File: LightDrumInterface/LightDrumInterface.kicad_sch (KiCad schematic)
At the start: 79 parts, among them J1 MIDI-IN, J2 0525593652, J2 Micro_SD_Card, J4 PWR-CONN, J5 MIDI-OUT, J6 0541323662, Q1 NX6008NBKWX, Q2 NX6008NBKWX, Q3 NX6008NBKWX, Q4 NX6008NBKWX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

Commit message: PCB Lock REV11
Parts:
- removed D-MD1, D-ML1, D-MR1, D-MU1: RED, LED_SMD:LED_0805_2012Metric, symbol Device:LED_Small
- added D2, D3: APHBM2012QBDSURKC, Daxxn_LEDs:APHBM-2012, symbol Daxxn_LEDs:APHBM2012QBDSURKC
- added H1, H2, H3, H4: M2.5, MountingHole:MountingHole_2.7mm_M2.5_Pad_Via, symbol Mechanical:MountingHole_Pad
- DA1: PartNumber (none) -> 0904-0001
- J2: value 0525593652 -> DNP; SupplierPN (none) -> WM7988CT-ND
- U4: PartNumber (none) -> 0802-0002
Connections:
- net SD-DAT0 is gone; now on net SD-D0: J2.7 (DAT0), R25.2
- net SD-DAT3/CD is gone; now on net SD-CD: J2.2 (DAT3/CD), R27.2
- net AUDIO-SRC-IND: now also J2.3 (Pin_3); no longer J2.4 (Pin_4)
- net DIAG-DEBUG: no longer J2.5 (Pin_5)
- net DIAG-STATUS: no longer J2.6 (Pin_6)
- net ENC1-A: now also J2.21 (Pin_21), J6.16 (Pin_16); no longer J2.28 (Pin_28), J6.9 (Pin_9)
- net ENC1-B: now also J2.14 (Pin_14), J6.23 (Pin_23); no longer J2.10 (Pin_10), J6.27 (Pin_27)
- net ENC2-A: now also J2.23 (Pin_23), J6.14 (Pin_14); no longer J2.26 (Pin_26), J6.11 (Pin_11)
- net ENC2-SW: now also J2.19 (Pin_19), J6.18 (Pin_18); no longer J2.22 (Pin_22), J6.15 (Pin_15)
- net GND: now also J2.32 (Pin_32), J6.5 (Pin_5), H1.1, H2.1, H3.1, H4.1; no longer J2.3 (Pin_3), J2.30 (Pin_30), J2.34 (Pin_34), J2.8 (Pin_8), J2.9 (Pin_9), J6.7 (Pin_7)
- net GRAPH-CLK: now also J6.6 (Pin_6); no longer J2.29 (Pin_29), J6.8 (Pin_8)
- net GRAPH-LE: now also J6.25 (Pin_25); no longer J2.14 (Pin_14), J6.23 (Pin_23)
- net GRAPH-SDI: now also J6.24 (Pin_24); no longer J2.31 (Pin_31), J6.6 (Pin_6)
- net GRAPH-~{OE}: now also J6.27 (Pin_27); no longer J2.12 (Pin_12), J6.25 (Pin_25)
- net I2C-SCLK: now also J6.15 (Pin_15); no longer J2.20 (Pin_20), J6.17 (Pin_17)
- net I2C-SDA: now also J6.13 (Pin_13); no longer J2.23 (Pin_23), J6.14 (Pin_14)
- net MENU-ACT: no longer J2.17 (Pin_17)
- net MENU-BACK: no longer J2.16 (Pin_16)
- net MENU-DOWN: no longer J2.11 (Pin_11)
- net MENU-LEFT: now also J6.8 (Pin_8); no longer J2.13 (Pin_13), J6.24 (Pin_24)
- net MENU-RIGHT: no longer J2.18 (Pin_18)
- net MENU-UP: no longer J2.15 (Pin_15)
- net MIDI-IN: now also J6.3 (Pin_3); no longer J2.32 (Pin_32), J6.5 (Pin_5)
- net MIDI-OUT: no longer J2.35 (Pin_35)
- net SCR-RX: now also J6.9 (Pin_9); no longer J2.19 (Pin_19), J6.18 (Pin_18)
- net SCR-TX: now also J6.7 (Pin_7); no longer J2.21 (Pin_21), J6.16 (Pin_16)
- net SD-CD: now also J6.17 (Pin_17); no longer J6.3 (Pin_3)
- net SD-CLK: now also J6.28 (Pin_28); no longer J6.29 (Pin_29)
- net SD-D0: now also J6.29 (Pin_29); no longer J6.28 (Pin_28)
- net STRIP-PWR: now also J2.6 (Pin_6); no longer J2.7 (Pin_7)
- net VCC: now also J2.26 (Pin_26), J6.11 (Pin_11), D2.1 (B-A), D2.4 (R-A), D3.1 (B-A), D3.4 (R-A); no longer J2.24 (Pin_24), J6.13 (Pin_13)
- net ~{RESET}: no longer J2.33 (Pin_33)
- net at U1.17 (~{OUT12}): now also D2.2 (B-K)
- net at U1.18 (~{OUT13}): now also D2.3 (R-K)
- net at DA1.11: now also U1.14 (~{OUT9}); no longer U1.13 (~{OUT8})
- net at U1.15 (~{OUT10}): now also D3.2 (B-K)
- net at DA1.12: now also U1.13 (~{OUT8}); no longer U1.14 (~{OUT9})
- net at U1.16 (~{OUT11}): now also D3.3 (R-K)
- new net DIAG-DEBUG_{PWM}: J2.4 (Pin_4)
- new net DIAG-STATUS_{PWM}: J2.5 (Pin_5)
- new net GRAPH-CLK_{S}: J2.31 (Pin_31)
- new net GRAPH-LE_{S}: J2.12 (Pin_12)
- new net GRAPH-SDI_{S}: J2.13 (Pin_13)
- new net GRAPH-~{OE}_{S}: J2.10 (Pin_10)
- new net I2C-SCLK_{S}: J2.22 (Pin_22)
- new net I2C-SDA_{S}: J2.24 (Pin_24)
- new net MENU-ACT_{INT}: J2.17 (Pin_17)
- new net MENU-BACK_{INT}: J2.16 (Pin_16)
- new net MENU-DOWN_{INT}: J2.11 (Pin_11)
- new net MENU-LEFT_{INT}: J2.29 (Pin_29)
- new net MENU-RIGHT_{INT}: J2.18 (Pin_18)
- new net MENU-UP_{INT}: J2.15 (Pin_15)
- new net MIDI-IN_{S}: J2.34 (Pin_34)
- new net MIDI-OUT_{S}: J2.35 (Pin_35)
- new net SCR-RX_{S}: J2.28 (Pin_28)
- new net SCR-TX_{S}: J2.30 (Pin_30)
- new net SD-CD_{S}: J2.20 (Pin_20)
- new net SD-CLK_{S}: J2.9 (Pin_9)
- new net SD-CMD_{S}: J2.7 (Pin_7)
- new net SD-D0_{S}: J2.8 (Pin_8)
- new net ~{RESET}_{C}: J2.33 (Pin_33)
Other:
- note added: "ENCODER SELECT"
- note added: "MATCHING CONN ON MAIN PCB -NOT POPULATED-"
- note removed: "MATCHING CONN ON MAIN PCB NOT POPULATED"
- moved on the sheet: DA1I, DA1J

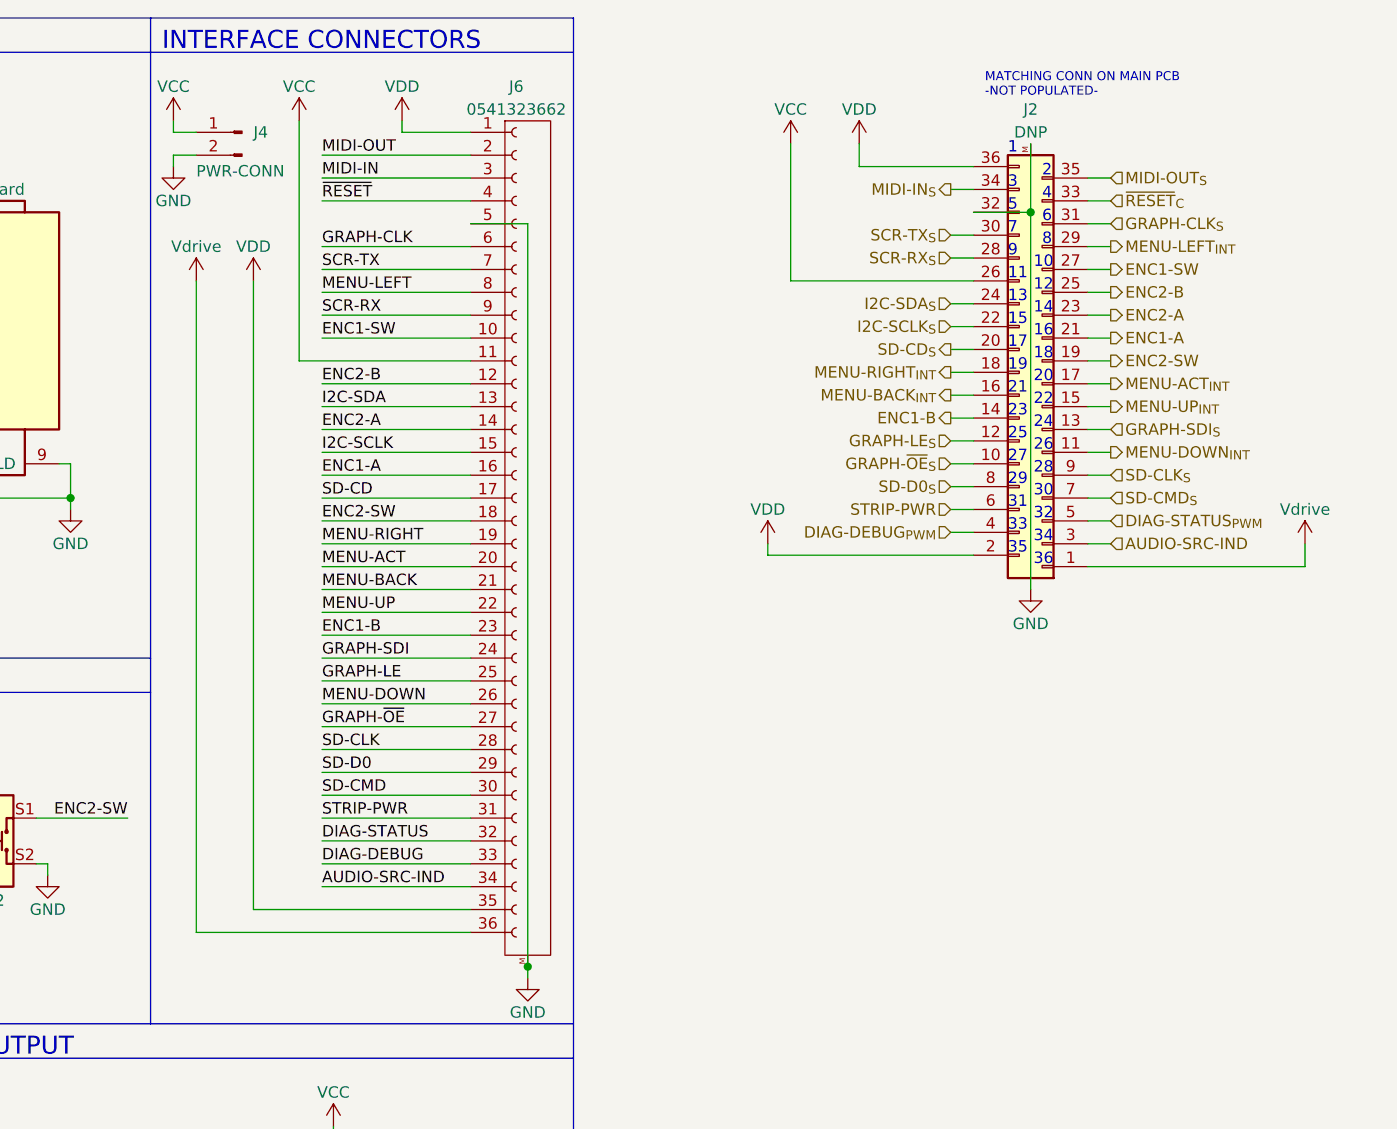
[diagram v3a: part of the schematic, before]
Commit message: Fix backwards Connector - Initial Testing
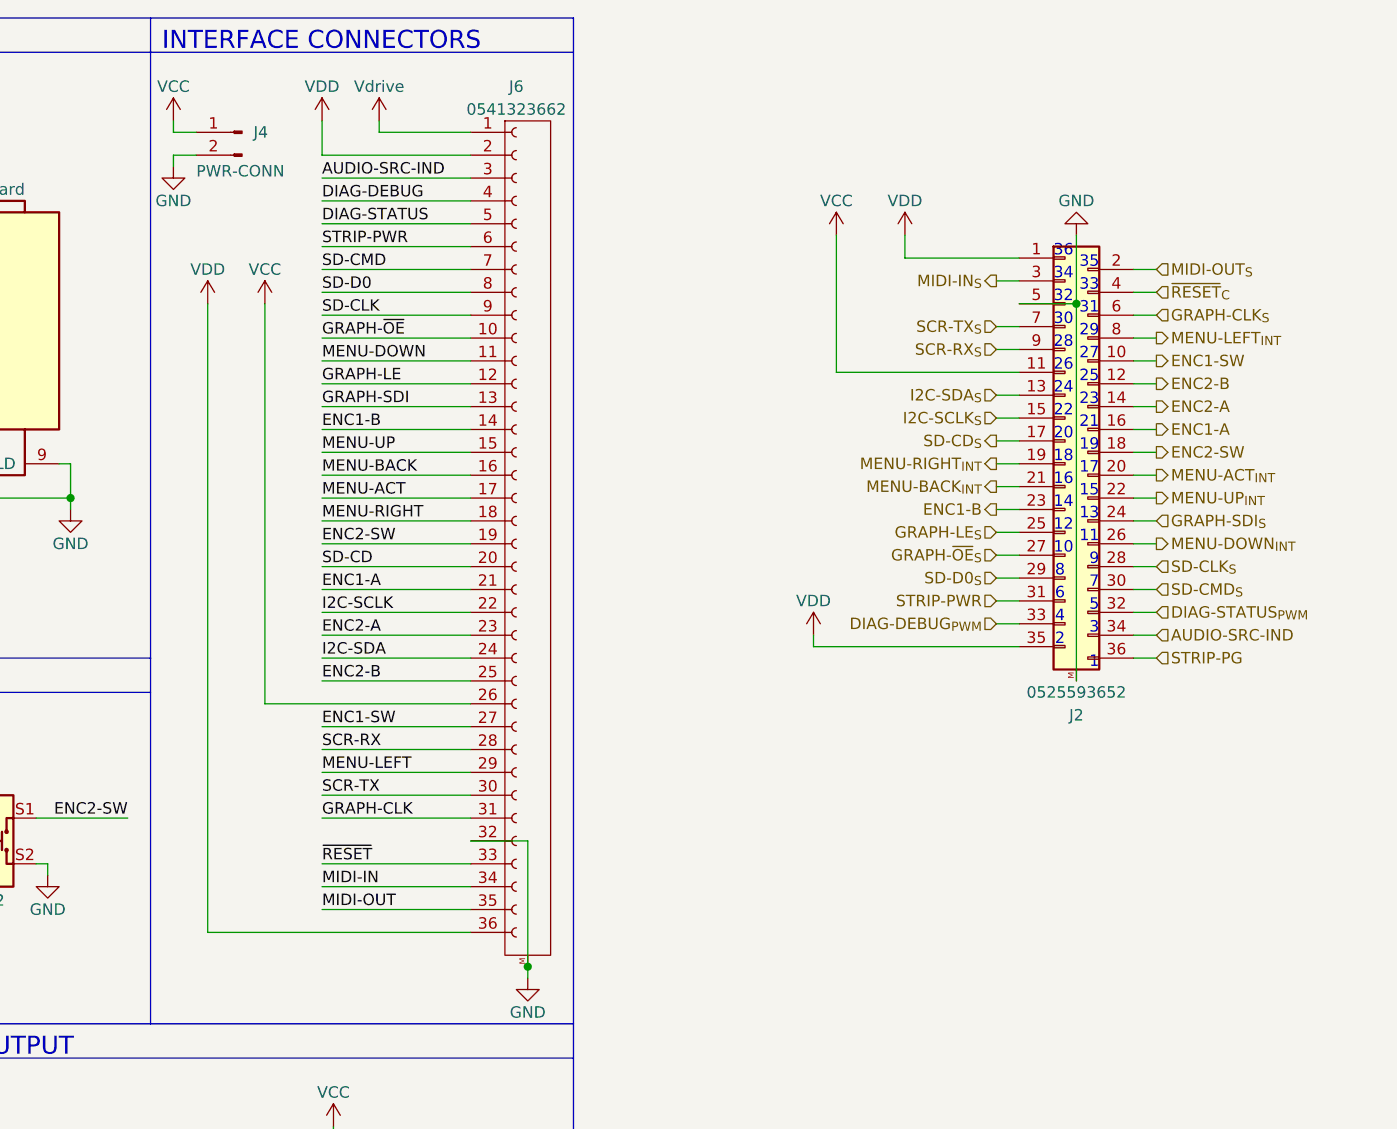
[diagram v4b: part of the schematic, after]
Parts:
- J2: value DNP -> 0525593652
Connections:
- net AUDIO-SRC-IND: now also J2.34 (Pin_34), J6.3 (Pin_3); no longer J2.3 (Pin_3), J6.34 (Pin_34)
- net DIAG-DEBUG: now also J6.4 (Pin_4); no longer J6.33 (Pin_33)
- net DIAG-DEBUG_{PWM}: now also J2.33 (Pin_33); no longer J2.4 (Pin_4)
- net DIAG-STATUS: now also J6.5 (Pin_5); no longer J6.32 (Pin_32)
- net DIAG-STATUS_{PWM}: now also J2.32 (Pin_32); no longer J2.5 (Pin_5)
- net ENC1-A: now also J2.16 (Pin_16), J6.21 (Pin_21); no longer J2.21 (Pin_21), J6.16 (Pin_16)
- net ENC1-B: now also J2.23 (Pin_23), J6.14 (Pin_14); no longer J2.14 (Pin_14), J6.23 (Pin_23)
- net ENC1-SW: now also J2.10 (Pin_10), J6.27 (Pin_27); no longer J2.27 (Pin_27), J6.10 (Pin_10)
- net ENC2-A: now also J2.14 (Pin_14), J6.23 (Pin_23); no longer J2.23 (Pin_23), J6.14 (Pin_14)
- net ENC2-B: now also J2.12 (Pin_12), J6.25 (Pin_25); no longer J2.25 (Pin_25), J6.12 (Pin_12)
- net ENC2-SW: now also J2.18 (Pin_18), J6.19 (Pin_19); no longer J2.19 (Pin_19), J6.18 (Pin_18)
- net GND: now also J2.5 (Pin_5), J6.32 (Pin_32); no longer J2.32 (Pin_32), J6.5 (Pin_5)
- net GRAPH-CLK: now also J6.31 (Pin_31); no longer J6.6 (Pin_6)
- net GRAPH-CLK_{S}: now also J2.6 (Pin_6); no longer J2.31 (Pin_31)
- net GRAPH-LE: now also J6.12 (Pin_12); no longer J6.25 (Pin_25)
- net GRAPH-LE_{S}: now also J2.25 (Pin_25); no longer J2.12 (Pin_12)
- net GRAPH-SDI: now also J6.13 (Pin_13); no longer J6.24 (Pin_24)
- net GRAPH-SDI_{S}: now also J2.24 (Pin_24); no longer J2.13 (Pin_13)
- net GRAPH-~{OE}: now also J6.10 (Pin_10); no longer J6.27 (Pin_27)
- net GRAPH-~{OE}_{S}: now also J2.27 (Pin_27); no longer J2.10 (Pin_10)
- net I2C-SCLK: now also J6.22 (Pin_22); no longer J6.15 (Pin_15)
- net I2C-SCLK_{S}: now also J2.15 (Pin_15); no longer J2.22 (Pin_22)
- net I2C-SDA: now also J6.24 (Pin_24); no longer J6.13 (Pin_13)
- net I2C-SDA_{S}: now also J2.13 (Pin_13); no longer J2.24 (Pin_24)
- net MENU-ACT: now also J6.17 (Pin_17); no longer J6.20 (Pin_20)
- net MENU-ACT_{INT}: now also J2.20 (Pin_20); no longer J2.17 (Pin_17)
- net MENU-BACK: now also J6.16 (Pin_16); no longer J6.21 (Pin_21)
- net MENU-BACK_{INT}: now also J2.21 (Pin_21); no longer J2.16 (Pin_16)
- net MENU-DOWN: now also J6.11 (Pin_11); no longer J6.26 (Pin_26)
- net MENU-DOWN_{INT}: now also J2.26 (Pin_26); no longer J2.11 (Pin_11)
- net MENU-LEFT: now also J6.29 (Pin_29); no longer J6.8 (Pin_8)
- net MENU-LEFT_{INT}: now also J2.8 (Pin_8); no longer J2.29 (Pin_29)
- net MENU-RIGHT: now also J6.18 (Pin_18); no longer J6.19 (Pin_19)
- net MENU-RIGHT_{INT}: now also J2.19 (Pin_19); no longer J2.18 (Pin_18)
- net MENU-UP: now also J6.15 (Pin_15); no longer J6.22 (Pin_22)
- net MENU-UP_{INT}: now also J2.22 (Pin_22); no longer J2.15 (Pin_15)
- net MIDI-IN: now also J6.34 (Pin_34); no longer J6.3 (Pin_3)
- net MIDI-IN_{S}: now also J2.3 (Pin_3); no longer J2.34 (Pin_34)
- net MIDI-OUT: now also J6.35 (Pin_35); no longer J6.2 (Pin_2)
- net MIDI-OUT_{S}: now also J2.2 (Pin_2); no longer J2.35 (Pin_35)
- net SCR-RX: now also J6.28 (Pin_28); no longer J6.9 (Pin_9)
- net SCR-RX_{S}: now also J2.9 (Pin_9); no longer J2.28 (Pin_28)
- net SCR-TX: now also J6.30 (Pin_30); no longer J6.7 (Pin_7)
- net SCR-TX_{S}: now also J2.7 (Pin_7); no longer J2.30 (Pin_30)
- net SD-CD: now also J6.20 (Pin_20); no longer J6.17 (Pin_17)
- net SD-CD_{S}: now also J2.17 (Pin_17); no longer J2.20 (Pin_20)
- net SD-CLK: now also J6.9 (Pin_9); no longer J6.28 (Pin_28)
- net SD-CLK_{S}: now also J2.28 (Pin_28); no longer J2.9 (Pin_9)
- net SD-CMD: now also J6.7 (Pin_7); no longer J6.30 (Pin_30)
- net SD-CMD_{S}: now also J2.30 (Pin_30); no longer J2.7 (Pin_7)
- net SD-D0: now also J6.8 (Pin_8); no longer J6.29 (Pin_29)
- net SD-D0_{S}: now also J2.29 (Pin_29); no longer J2.8 (Pin_8)
- net STRIP-PWR: now also J2.31 (Pin_31), J6.6 (Pin_6); no longer J2.6 (Pin_6), J6.31 (Pin_31)
- net VCC: now also J2.11 (Pin_11), J6.26 (Pin_26); no longer J2.26 (Pin_26), J6.11 (Pin_11)
- net VDD: now also J2.1 (Pin_1), J2.35 (Pin_35), J6.2 (Pin_2), J6.36 (Pin_36); no longer J2.2 (Pin_2), J2.36 (Pin_36), J6.1 (Pin_1), J6.35 (Pin_35)
- net Vdrive: now also J6.1 (Pin_1); no longer J2.1 (Pin_1), J6.36 (Pin_36)
- net ~{RESET}: now also J6.33 (Pin_33); no longer J6.4 (Pin_4)
- net ~{RESET}_{C}: now also J2.4 (Pin_4); no longer J2.33 (Pin_33)
- new net STRIP-PG: J2.36 (Pin_36)
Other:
- note removed: "MATCHING CONN ON MAIN PCB -NOT POPULATED-"

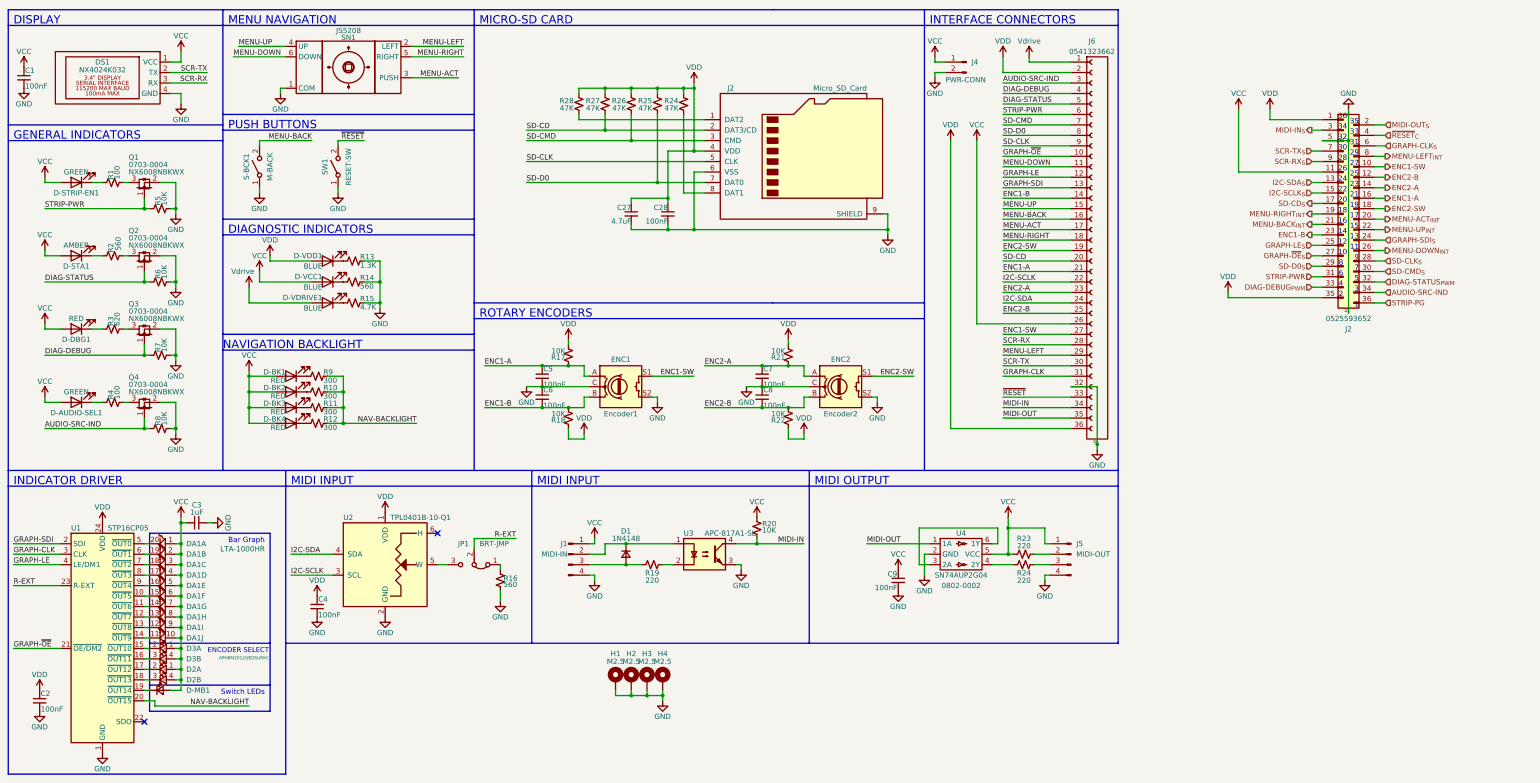
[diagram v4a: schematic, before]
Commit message: Organize old files and generate interface gerbers
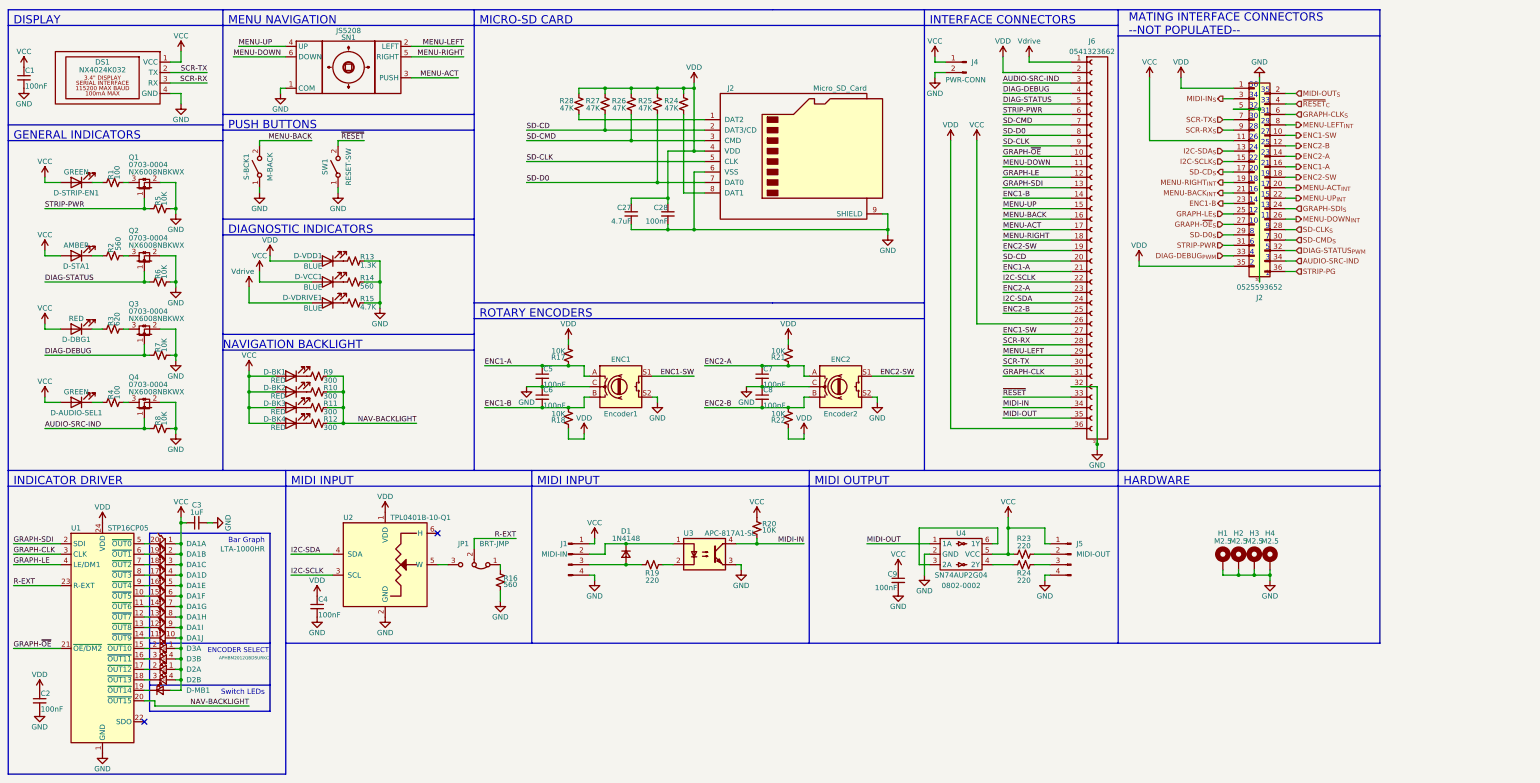
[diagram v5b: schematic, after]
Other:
- note added: "HARDWARE"
- note added: "MATING INTERFACE CONNECTORS --NOT POPULATED--"
- moved on the sheet: H1, H2, H3, H4
